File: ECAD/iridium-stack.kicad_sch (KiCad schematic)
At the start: 31 parts

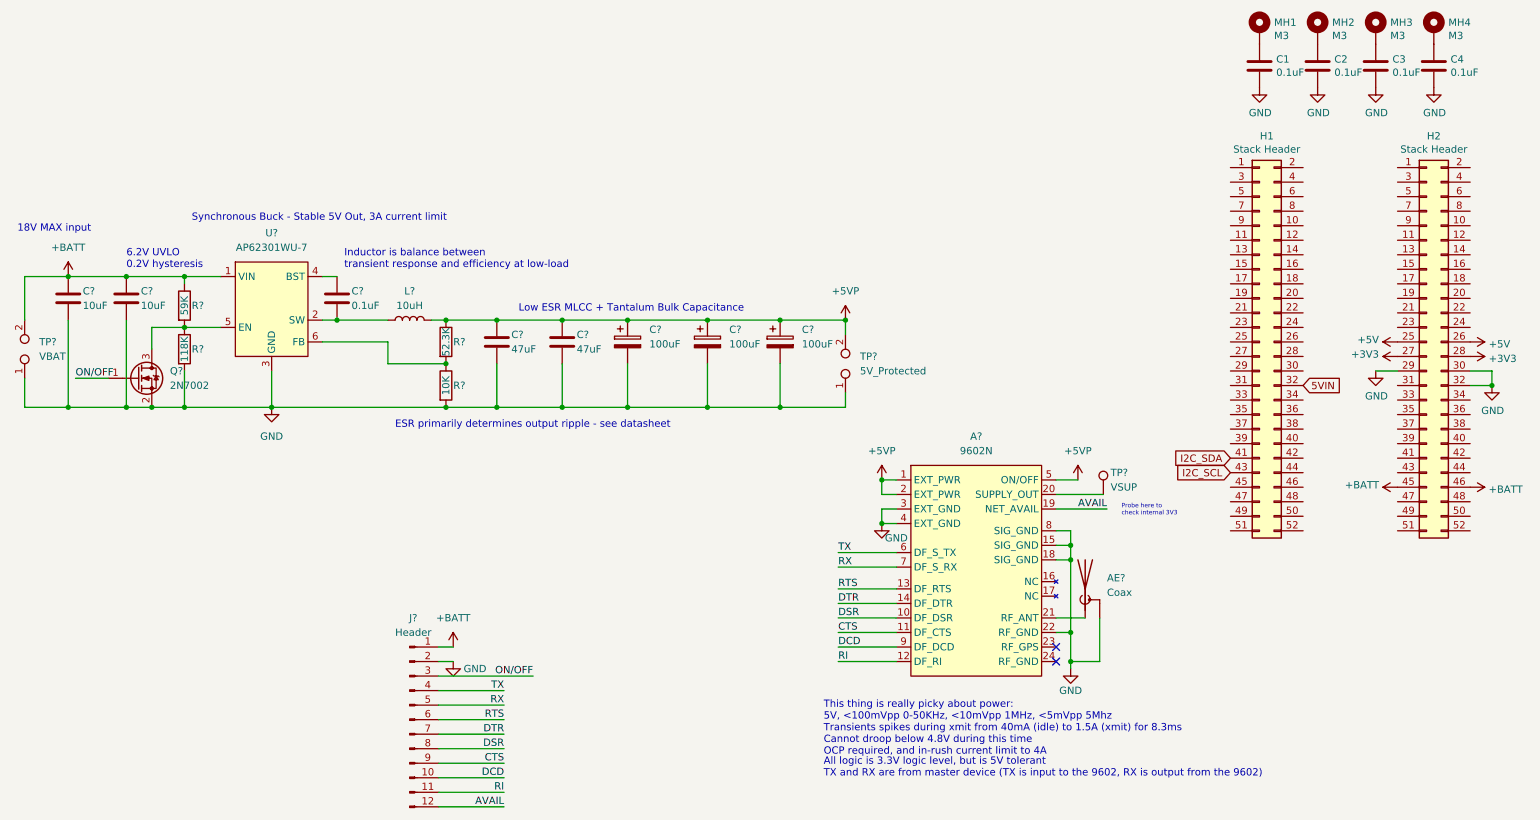
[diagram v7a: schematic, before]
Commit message: Replace AP62301 with MAX17644
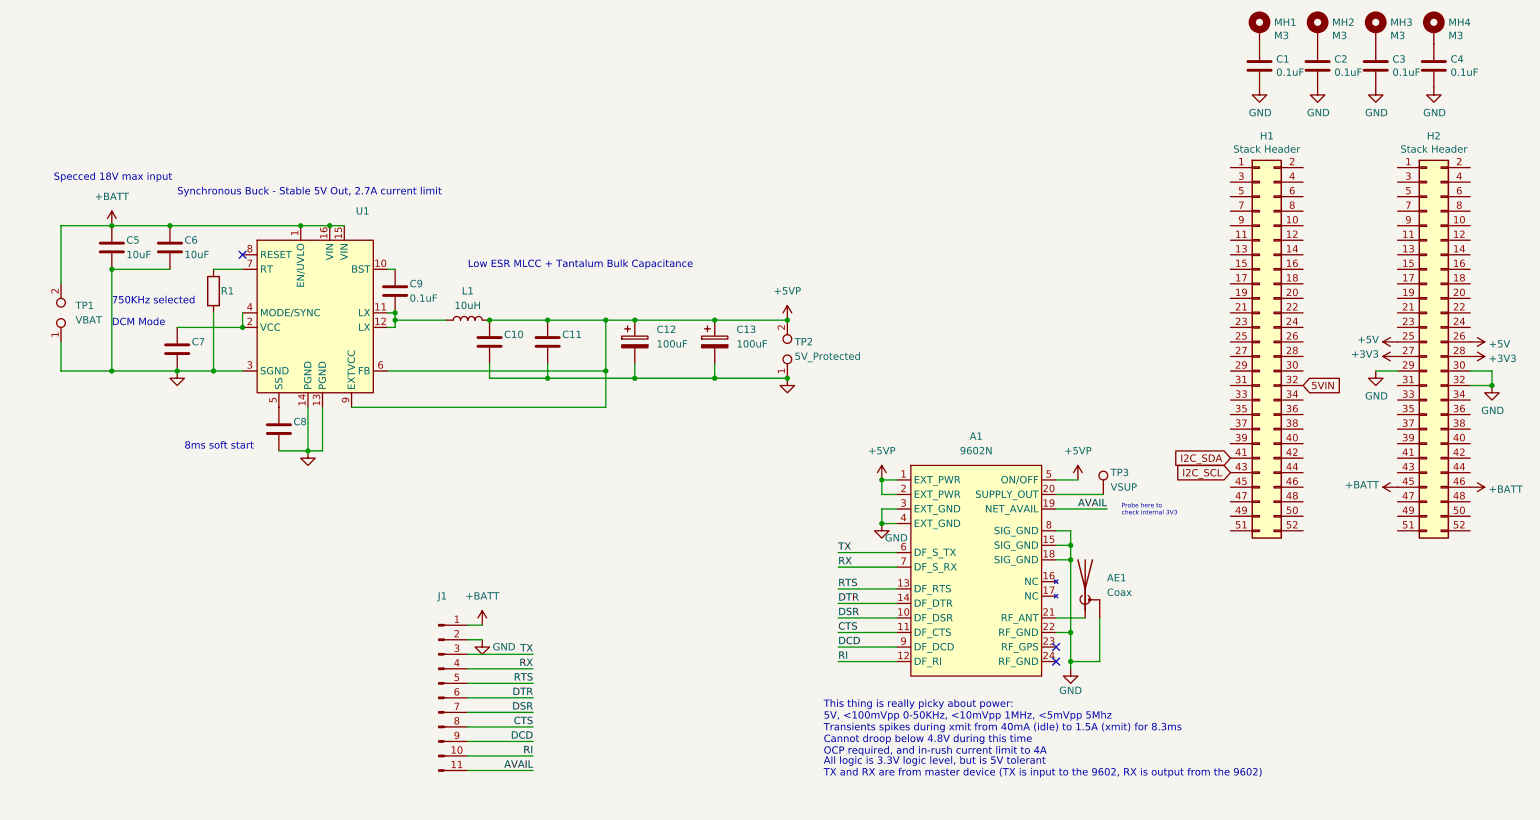
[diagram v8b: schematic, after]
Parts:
- removed C?: 100uF, symbol Device:C_Polarized
- removed J?: Header, symbol Connector:Conn_01x12_Male
- removed Q?: 2N7002, Package_TO_SOT_SMD:SOT-23, symbol Transistor_FET:2N7002
- removed R?: 10K, symbol Device:R
- removed R?: 118K, symbol Device:R
- removed R?: 59K, symbol Device:R
- removed R?: 52.3K, symbol Device:R
- removed U?: AP62301WU-7, symbol Symbols:AP62301WU-7
- added C7, C8: (no value), symbol Device:C
- added J1: (no value), symbol Connector:Conn_01x11_Male
- added R1: (no value), symbol Device:R
- added U1: (no value), symbol Symbols:MAX17644
- C10, C11: renamed from C?; value 47uF -> (none)
- gave numbers to parts that had none: 11
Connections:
- net +5VP: now also U1.6 (FB), U1.9 (EXTVCC)
- net +BATT: now also J1.1 (Pin_1), U1.1 (EN/UVLO), U1.15 (VIN), U1.16 (VIN)
- net AVAIL: now also J1.11 (Pin_11)
- net CTS: now also J1.8 (Pin_8)
- net DCD: now also J1.9 (Pin_9)
- net DSR: now also J1.7 (Pin_7)
- net DTR: now also J1.6 (Pin_6)
- net GND: now also C7.2, C8.2, J1.2 (Pin_2), R1.2, U1.13 (PGND), U1.14 (PGND), U1.3 (SGND)
- net RI: now also J1.10 (Pin_10)
- net RTS: now also J1.5 (Pin_5)
- net RX: now also J1.4 (Pin_4)
- net TX: now also J1.3 (Pin_3)
- net at C9.1: now also U1.10 (BST)
- net at C9.2, L1.1: now also U1.11 (LX), U1.12 (LX)
- new net: R1.1, U1.7 (RT)
- new net: C7.1, U1.2 (VCC), U1.4 (MODE/SYNC)
- new net: C8.1, U1.5 (SS)
- no-connect marks 2 -> 3
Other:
- note added: "750KHz selected"
- note added: "8ms soft start"
- note added: "DCM Mode"
- note added: "Specced 18V max input"
- note added: "Synchronous Buck - Stable 5V Out, 2.7A current limit"
- note removed: "18V MAX input"
- note removed: "6.2V UVLO 0.2V hysteresis"
- note removed: "ESR primarily determines output ripple - see datasheet"
- note removed: "Inductor is balance between transient response and efficiency at low-load"
- note removed: "Synchronous Buck - Stable 5V Out, 3A current limit"
- moved on the sheet: C10, C11, C12, C13, C5, C6, C9, L1, TP1, TP2
